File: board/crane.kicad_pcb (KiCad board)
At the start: 4 copper layers, 71 x 169 mm, 80 parts, among them IC1 PMV48XP, J1 USB-B-S-X-X-TH, J10 AVR-ISP-6, J8 AVR-ISP-6, SW1 SW_Push, SW10 SW_Push, SW11 SW_Push, SW12 SW_Push, SW2 SW_Push, SW3 SW_Push, SW4 SW_Push, SW5 SW_Push, SW6 SW_Push, SW7 SW_Push, SW8 SW_Push, SW9 SW_Push, U1 Waveshare_LCD_Module_2.4in, U2 LMV358IDT, U3 ATmega2560-16A, U4 LD1117S50TR_SOT223, U5 LP2985-3.3, U6 ATmega16U2-A, Y1 CSTCE16M0V53-R0, Y2 Crystal

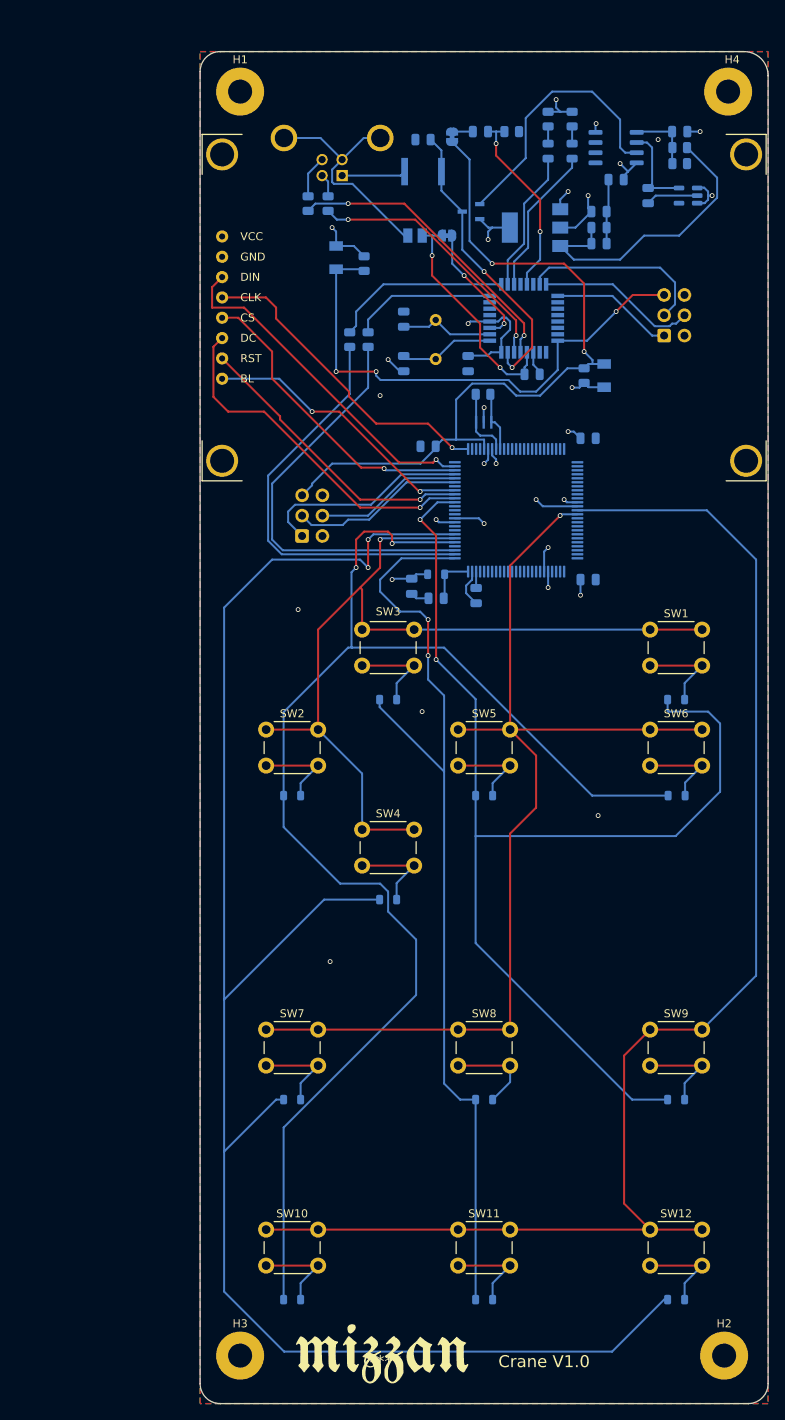
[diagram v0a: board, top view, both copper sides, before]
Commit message: updated to Crane V2 Rev A
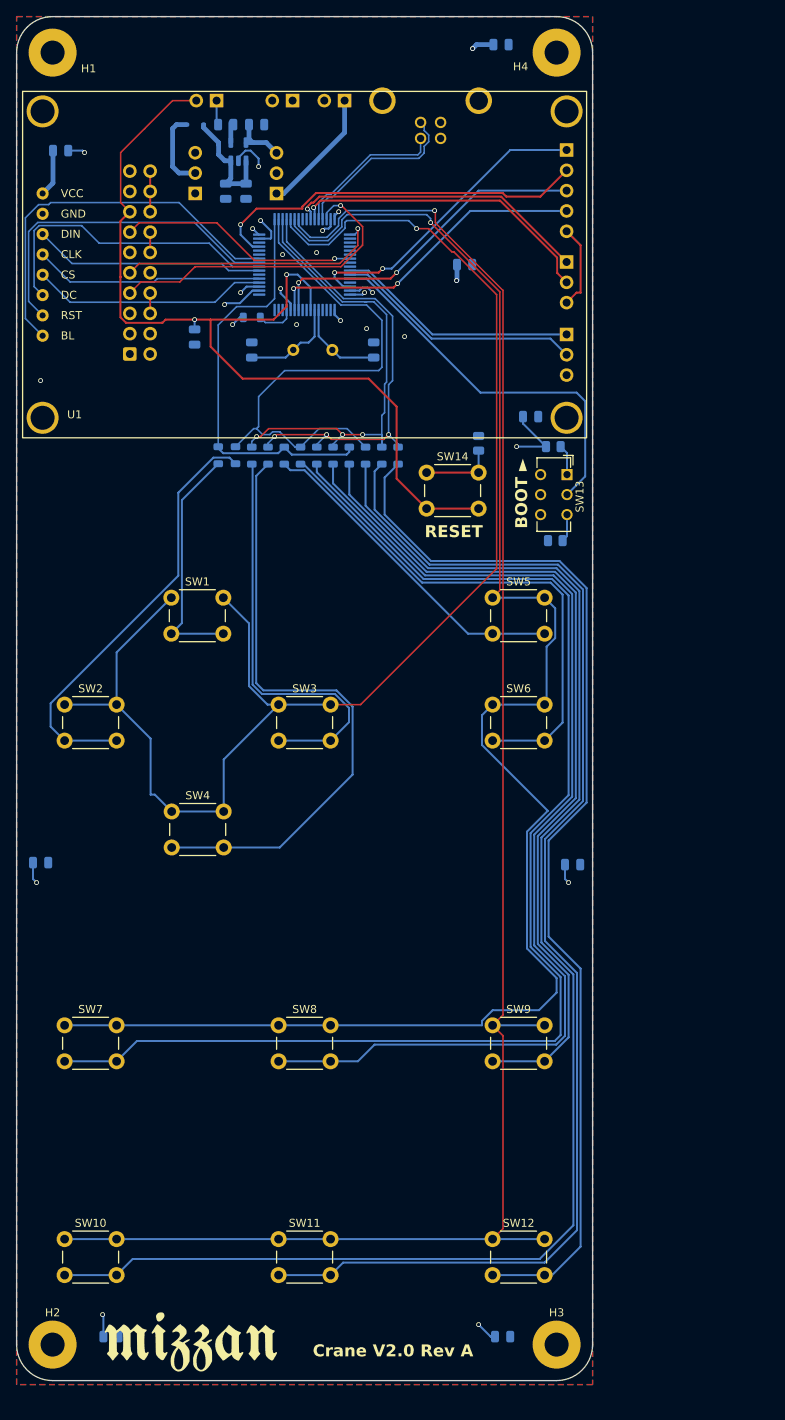
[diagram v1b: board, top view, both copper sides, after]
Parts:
- removed C16: 1uF, Capacitor_SMD:C_0805_2012Metric
- removed C17, C18: 100nF, Capacitor_SMD:C_0805_2012Metric
- removed D14: CD1206-S01575, footprints:DIOC3215X95N
- removed D15: LED_RX, LED_SMD:LED_0805_2012Metric
- removed D16: LED_TX, LED_SMD:LED_0805_2012Metric
- removed F1: MF-MSMF050-2, footprints:FUSC4632X85N
- removed IC1: PMV48XP, footprints:SOT95P230X110-3N
- removed JP1: GROUND, Jumper:SolderJumper-2_P1.3mm_Bridged_RoundedPad1.0x1.5mm
- removed JP2: RESET-EN, Jumper:SolderJumper-2_P1.3mm_Bridged_RoundedPad1.0x1.5mm
- removed L1: 10uH, Inductor_SMD:L_0805_2012Metric
- removed R10, R11, R12, R8, R9: 1K, Resistor_SMD:R_0805_2012Metric
- removed R4, R7: 10K, Resistor_SMD:R_0805_2012Metric
- removed R5, R6: 22, Resistor_SMD:R_0805_2012Metric
- removed U4: LD1117S50TR_SOT223, Package_TO_SOT_SMD:SOT-223-3_TabPin2
- removed U5: LP2985-3.3, Package_TO_SOT_SMD:SOT-23-5
- removed U6: ATmega16U2-A, Package_QFP:TQFP-32_7x7mm_P0.8mm
- removed Y1: CSTCE16M0V53-R0, footprints:CSTCE16M0V53R0
- removed Y2: Crystal, Crystal:Crystal_HC49-4H_Vertical
- added J11: Conn_01x05, Connector_PinHeader_2.54mm:PinHeader_1x05_P2.54mm_Vertical, B.Cu at (160.3, 99.3)
- added J3: Conn_01x03_Male, Connector_PinHeader_2.54mm:PinHeader_1x03_P2.54mm_Vertical, B.Cu at (124.0, 104.7)
- added J4: Conn_01x02_Male, Connector_PinHeader_2.54mm:PinHeader_1x02_P2.54mm_Horizontal, B.Cu at (126.1, 93.1)
- added J5: Conn_01x02_Male, Connector_PinHeader_2.54mm:PinHeader_1x02_P2.54mm_Horizontal, B.Cu at (132.6, 93.1)
- added J6: Conn_01x03_Male, Connector_PinHeader_2.54mm:PinHeader_1x03_P2.54mm_Vertical, B.Cu at (113.9, 104.7)
- added J7: 292304-1, footprints:TE_292304-1, B.Cu at (143.3, 93.1)
- added J9: Conn_01x03, Connector_PinHeader_2.54mm:PinHeader_1x03_P2.54mm_Vertical, B.Cu at (160.3, 113.3)
- added SW13: SW_Push_DPDT, Button_Switch_THT:SW_CuK_JS202011CQN_DPDT_Straight, F.Cu at (160.4, 139.9)
- added SW14: SW_Push, Button_Switch_THT:SW_PUSH_6mm_H9.5mm, F.Cu at (142.8, 139.6)
- added e1: 9B-16.000MAAE-B, Crystal:Crystal_HC49-U_Vertical, B.Cu at (131.0, 124.3)
- C10: value 47uF -> 1uF
- C11: value 22pF -> 10uF
- C12: value 1uF -> 1uF_X5R
- C14: value 22pF -> 10nF_X7R
- C15: value 22pF -> 1uF
- C2, C3: value 100nF -> 20pF
- C4, C5: value 100nF -> 10nF
- C8, C9: value 47uF -> 100nF
- D13: value CD1206-S01575 -> BAT60AE6327HTSA1; footprint footprints:DIOC3215X95N -> Diode_SMD:D_SOD-323
- FB1: value MH2029-300Y -> HZ0805E601R-10; footprint footprints:BEADC2016X130N -> Inductor_SMD:L_0805_2012Metric
- J1: value USB-B-S-X-X-TH -> Conn_01x02_Male; footprint footprints:SAMTEC_USB-B-S-X-X-TH -> Connector_PinHeader_2.54mm:PinHeader_1x02_P2.54mm_Horizontal
- J10: value AVR-ISP-6 -> Conn_01x03; footprint Connector_IDC:IDC-Header_2x03_P2.54mm_Vertical -> Connector_PinHeader_2.54mm:PinHeader_1x03_P2.54mm_Vertical
- J8: value AVR-ISP-6 -> Conn_ARM_JTAG_SWD_20; footprint Connector_IDC:IDC-Header_2x03_P2.54mm_Vertical -> Connector_IDC:IDC-Header_2x10_P2.54mm_Vertical
- R1: value 1M -> 10K
- R3: value 10K -> 100
- U2: value LMV358IDT -> STM32L476RGT6; footprint Package_SO:SO-8_3.9x4.9mm_P1.27mm -> Package_QFP:LQFP-64_10x10mm_P0.5mm
- U3: value ATmega2560-16A -> LD3985M33R_SOT23; footprint Package_QFP:TQFP-100_14x14mm_P0.5mm -> Package_TO_SOT_SMD:SOT-23-5
- moved C10 153.3 mm to (103.4, 247.6)
- moved C11 111.7 mm to (152.3, 247.6)
- moved D12 111.1 mm to (139.2, 137.5), turned to -90 degrees
- moved D11 106.3 mm to (137.2, 137.5), turned to -90 degrees
- moved D10 105.9 mm to (135.2, 137.5), turned to -90 degrees
- moved D9 90.3 mm to (133.1, 137.5), turned to -90 degrees
- moved C7 86.6 mm to (94.6, 188.4)
- moved H2 84.0 mm to (96.1, 248.6)
- moved D8 82.7 mm to (131.1, 137.5), turned to -90 degrees
- moved D7 80.6 mm to (129.1, 137.5), turned to -90 degrees
- moved C4 69.9 mm to (97.1, 99.4), turned to 180 degrees
- moved D1 64.9 mm to (116.8, 137.5), turned to -90 degrees
- moved D6 63.4 mm to (127.1, 137.5), turned to -90 degrees
- moved C3 60.1 mm to (121.0, 124.3), turned to -90 degrees
- moved SW1 60.0 mm to (110.9, 155.3)
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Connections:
- C1 pad 2: +5V -> NRST
- C10 pad 2: +5V -> +3V3
- C11 pad 1: RESET -> GND
- C11 pad 2: GND -> +3V3
- C12 pad 2: +3V3 -> Net-(D13-K)
- C13 pad 1: USBVCC -> GND
- C13 pad 2: GND -> Net-(D13-K)
- C14 pad 2: Net-(C14-Pad2) -> Net-(U3-BYP)
- C15 pad 2: Net-(C15-Pad2) -> 3.3V_REG
- C2 pad 2: Net-(C2-Pad2) -> Net-(U2-PH0)
- C3 pad 2: Net-(C3-Pad2) -> Net-(U2-PH1)
- C4 pad 2: +5V -> +3V3
- C5 pad 2: Net-(C5-Pad2) -> +3V3
- C6 pad 2: +5V -> +3V3
- C7 pad 2: +5V -> +3V3
- C8 pad 2: VIN -> +3V3
- C9 pad 2: VIN -> +3V3
- D13 pad 1: +5V -> Net-(D13-K)
- D13 pad 2: RESET -> +5V
- FB1 pad 1: Net-(FB1-Pad1) -> +3V3
- FB1 pad 2: Net-(C16-Pad1) -> Net-(U2-VDDA)
- J1 pad 1: /MCU/USBVCC_SOCKET -> GND
- J1 pad 2: /MCU/USB_D- -> NRST
- J10 pad 1: MISO2 -> I2C_SCL
- J10 pad 2: +5V -> I2C_SDA
- J10 pad 3: SCK2 -> GND
- J8 pad 1: MISO -> +3V3
- J8 pad 2: +5V -> unconnected-(J8-VCC/NC-Pad2)
- J8 pad 3: SCK -> unconnected-(J8-~{TRST}-Pad3)
- J8 pad 4: MOSI -> GND
- J8 pad 5: RESET -> unconnected-(J8-TDI-Pad5)
- R1 pad 1: Net-(R1-Pad1) -> +3V3
- R2 pad 1: Net-(C3-Pad2) -> Net-(R2-Pad1)
- R2 pad 2: VIN -> GND
- R3 pad 2: Net-(C3-Pad2) -> Net-(R3-Pad2)
- U1 pad 1: +5V -> +3V3
- U2 pad 1: unconnected-(U2-Pad1) -> +3V3
- U2 pad 4: GND -> unconnected-(U2-PC15-Pad4)
- U2 pad 5: Net-(C3-Pad2) -> Net-(U2-PH0)
- U2 pad 6: +3V3 -> Net-(U2-PH1)
- U2 pad 7: Net-(IC1-Pad1) -> NRST
- U2 pad 8: +5V -> unconnected-(U2-PC0-Pad8)
- U3 pad 1: SW_R2 -> Net-(D13-K)
- U3 pad 2: RX0 -> GND
- U3 pad 3: TX0 -> Net-(D13-K)
- U3 pad 4: unconnected-(U3-Pad4) -> Net-(U3-BYP)
- U3 pad 5: SW_R1 -> 3.3V_REG
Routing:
- net Net-(D10-A): track 11.7 -> 185.4 mm
- net SW_R3: track 217.0 -> 55.6 mm, vias 2 -> 3
- net Net-(D7-A): track 11.7 -> 160.7 mm
- net Net-(D11-A): track 11.7 -> 159.6 mm
- net Net-(D12-A): track 11.7 -> 134.5 mm
- net Net-(D8-A): track 11.7 -> 133.9 mm
- net NRST: track 0.00 -> 117.8 mm, vias 0 -> 2
- net SW_R1: track 176.9 -> 67.1 mm, vias 2 -> 0
- net Net-(D9-A): track 11.7 -> 107.1 mm
- net RESET: track 94.0 -> 0.00 mm, vias 2 -> 0
- net SW_R0: track 143.2 -> 51.8 mm, vias 2 -> 0
- net SW_C1: track 132.8 -> 205.6 mm
- net SW_C0: track 112.0 -> 180.6 mm
- net RESET2: track 65.9 -> 0.00 mm, vias 3 -> 0
- net Net-(D4-A): track 11.7 -> 76.1 mm
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- added copper zone on In1.Cu, net +3V3
- removed copper zone on In1.Cu, net +5V
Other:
- board size 71 x 169 mm -> 72 x 170.5 mm
- board text added: "3V3 SEL"
- board text added: "5V SEL"
- board text added: "BOOT ►"
- board text added: "Crane V2.0 Rev A"
- board text added: "GND"
- board text added: "MISO"
- board text added: "MOSI"
- board text added: "NSS"
- board text added: "RESET"
- board text added: "RX"
- board text added: "SCK"
- board text added: "SCL"
- board text added: "SDA"
- board text added: "TX"
- board text removed: "Crane V1.0"

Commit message: diode footprint change drom 0805 (2012) to SOD123
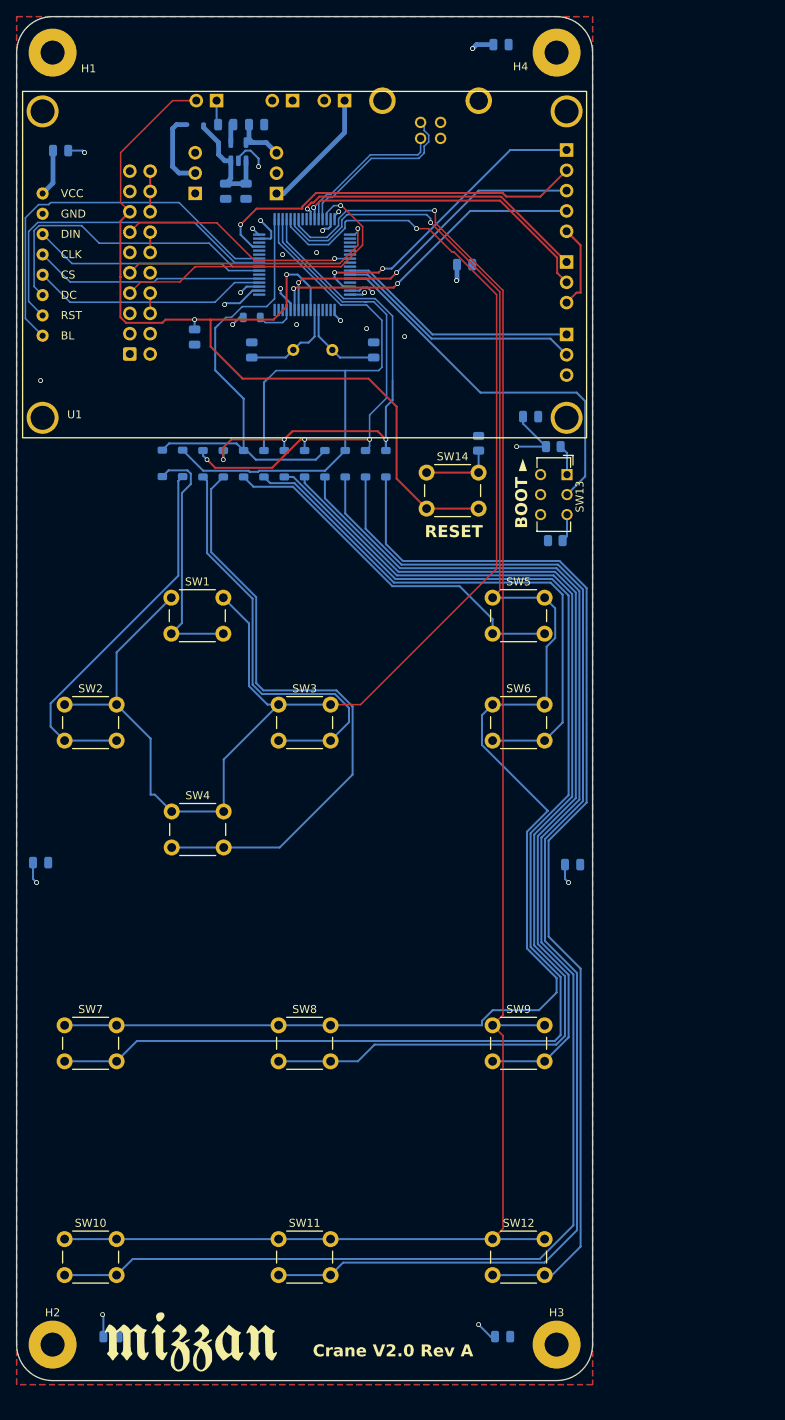
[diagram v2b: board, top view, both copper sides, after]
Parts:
- D1, D10, D11, D12, D2, D3, D4, D5, D6, D7, D8, D9: footprint Inductor_SMD:L_0805_2012Metric -> Diode_SMD:D_SOD-123
- moved D1 7.06 mm to (109.8, 138.5)
- moved D2 6.68 mm to (112.3, 138.5)
- moved D3 6.18 mm to (114.9, 138.5)
- moved D4 5.68 mm to (117.4, 138.5)
- moved D5 5.18 mm to (119.9, 138.5)
- moved D6 4.68 mm to (122.5, 138.5)
- moved D7 4.19 mm to (125.0, 138.5)
- moved D8 3.70 mm to (127.6, 138.5)
- moved D9 3.21 mm to (130.1, 138.5)
- moved D10 2.74 mm to (132.6, 138.5)
- moved D11 2.27 mm to (135.2, 138.5)
- moved D12 1.83 mm to (137.7, 138.5)
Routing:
- net SW_R1: track 67.1 -> 82.2 mm
- net SW_R3: track 55.6 -> 64.1 mm
- net Net-(D2-A): track 54.1 -> 47.1 mm
- net SW_R0: track 51.8 -> 57.6 mm
- net Net-(D5-A): track 41.3 -> 46.8 mm
- net SW_R2: track 58.2 -> 62.9 mm
- net Net-(D6-A): track 65.2 -> 69.1 mm
- net Net-(D7-A): track 160.7 -> 163.5 mm
- net Net-(D8-A): track 133.9 -> 135.9 mm
- net Net-(D9-A): track 107.1 -> 108.8 mm
- net Net-(D10-A): track 185.4 -> 186.9 mm
- net Net-(D1-A): track 30.2 -> 31.6 mm
- net Net-(D3-A): track 52.4 -> 53.3 mm
- net Net-(D4-A): track 76.1 -> 76.9 mm
- net Net-(D11-A): track 159.6 -> 160.1 mm
